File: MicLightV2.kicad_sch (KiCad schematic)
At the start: 73 parts, among them J1 12402012E212A, Q1 CSD87503Q3E, SW1 TL3365AF180QG, U1 UA78M33CKVURG3, U12 TC7PZ17FU, U2 AP33772DKZ-13, U3 STM32F072CBU6, Y1 16MHz

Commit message: REV1
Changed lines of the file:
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@@
 (kicad_sch
-	(version 20231120)
+	(version 20250114)
 	(generator "eeschema")
-	(generator_version "8.0")
+	(generator_version "9.0")
 	(paper "User" 286 260)
 	(title_block
@@
 		(company "Daxxn Industries")
 	)
+	(text "MCU GPIO"
+		(exclude_from_sim no)
+		(at 13.97 134.112 0)
+		(effects
+			(font
+				(size 2.5 2.5)
+				(thickness 0.254)
+				(bold yes)
+			)
+			(justify left)
+		)
+	)
+	(text "BUTTON FILTERING"
+		(exclude_from_sim no)
+		(at 157.226 176.276 0)
+		(effects
+			(font
+				(size 2.5 2.5)
+				(thickness 0.254)
+				(bold yes)
+			)
+			(justify left)
+		)
+	)
+	(text "INDICATORS"
+		(exclude_from_sim no)
+		(at 13.716 201.422 0)
+		(effects
+			(font
+				(size 2.5 2.5)
+				(thickness 0.254)
+				(bold yes)
+			)
+			(justify left)
+		)
+	)
+	(text "AUX POWER"
+		(exclude_from_sim no)
+		(at 186.436 16.256 0)
+		(effects
+			(font
+				(size 2.5 2.5)
+				(thickness 0.254)
+				(bold yes)
+			)
+			(justify left)
+		)
+	)
+	(text "LED DRIVERS"
+		(exclude_from_sim no)
+		(at 229.616 54.102 0)
+		(effects
+			(font
+				(size 2.5 2.5)
+				(thickness 0.254)
+				(bold yes)
+			)
+			(justify left)
+		)
+	)
+	(text "POTENTIOMETER"
+		(exclude_from_sim no)
+		(at 186.436 54.102 0)
+		(effects
+			(font
+				(size 2.5 2.5)
+				(thickness 0.254)
+				(bold yes)
+			)
+			(justify left)
+		)
+	)
+	(text "MCU POWER"
+		(exclude_from_sim no)
+		(at 157.226 97.282 0)
+		(effects
+			(font
+				(size 2.5 2.5)
+				(thickness 0.254)
+				(bold yes)
+			)
+			(justify left)
+		)
+	)
+	(text "USB POWER DELIVERY"
+		(exclude_from_sim no)
+		(at 16.51 15.24 0)
+		(effects
+			(font
+				(size 2.5 2.5)
+				(thickness 0.254)
+				(bold yes)
+			)
+			(justify left)
+		)
+	)
+	(text "MCU PROGRAMMING"
+		(exclude_from_sim no)
+		(at 13.716 97.282 0)
+		(effects
+			(font
+				(size 2.5 2.5)
+				(thickness 0.254)
+				(bold yes)
+			)
+			(justify left)
+		)
+	)
+	(text "MOUNT"
+		(exclude_from_sim no)
+		(at 128.016 201.422 0)
+		(effects
+			(font
+				(size 2.5 2.5)
+				(thickness 0.254)
+				(bold yes)
+			)
+			(justify left)
+		)
+	)
+	(text "BUTTONS"
+		(exclude_from_sim no)
+		(at 157.226 140.462 0)
+		(effects
+			(font
+				(size 2.5 2.5)
+				(thickness 0.254)
+				(bold yes)
+			)
+			(justify left)
+		)
+	)
 	(junction
 		(at 81.28 233.68)
@@
 		)
 	)
-	(text "MCU GPIO"
-		(exclude_from_sim no)
-		(at 13.97 134.112 0)
-		(effects
-			(font
-				(size 2.5 2.5)
-				(thickness 0.254)
-				(bold yes)
-			)
-			(justify left)
-		)
-	)
-	(text "BUTTON FILTERING"
-		(exclude_from_sim no)
-		(at 157.226 176.276 0)
-		(effects
-			(font
-				(size 2.5 2.5)
-				(thickness 0.254)
-				(bold yes)
-			)
-			(justify left)
-		)
-	)
-	(text "INDICATORS"
-		(exclude_from_sim no)
-		(at 13.716 201.422 0)
-		(effects
-			(font
-				(size 2.5 2.5)
-				(thickness 0.254)
-				(bold yes)
-			)
-			(justify left)
-		)
-	)
-	(text "AUX POWER"
-		(exclude_from_sim no)
-		(at 186.436 16.256 0)
-		(effects
-			(font
-				(size 2.5 2.5)
-				(thickness 0.254)
-				(bold yes)
-			)
-			(justify left)
-		)
-	)
-	(text "LED DRIVERS"
-		(exclude_from_sim no)
-		(at 229.616 54.102 0)
-		(effects
-			(font
-				(size 2.5 2.5)
-				(thickness 0.254)
-				(bold yes)
-			)
-			(justify left)
-		)
-	)
-	(text "POTENTIOMETER"
-		(exclude_from_sim no)
-		(at 186.436 54.102 0)
-		(effects
-			(font
-				(size 2.5 2.5)
-				(thickness 0.254)
-				(bold yes)
-			)
-			(justify left)
-		)
-	)
-	(text "MCU POWER"
-		(exclude_from_sim no)
-		(at 157.226 97.282 0)
-		(effects
-			(font
-				(size 2.5 2.5)
-				(thickness 0.254)
-				(bold yes)
-			)
-			(justify left)
-		)
-	)
-	(text "USB POWER DELIVERY"
-		(exclude_from_sim no)
-		(at 16.51 15.24 0)
-		(effects
-			(font
-				(size 2.5 2.5)
-				(thickness 0.254)
-				(bold yes)
-			)
-			(justify left)
-		)
-	)
-	(text "MCU PROGRAMMING"
-		(exclude_from_sim no)
-		(at 13.716 97.282 0)
-		(effects
-			(font
-				(size 2.5 2.5)
-				(thickness 0.254)
-				(bold yes)
-			)
-			(justify left)
-		)
-	)
-	(text "MOUNT"
-		(exclude_from_sim no)
-		(at 128.016 201.422 0)
-		(effects
-			(font
-				(size 2.5 2.5)
-				(thickness 0.254)
-				(bold yes)
-			)
-			(justify left)
-		)
-	)
-	(text "BUTTONS"
-		(exclude_from_sim no)
-		(at 157.226 140.462 0)
-		(effects
-			(font
-				(size 2.5 2.5)
-				(thickness 0.254)
-				(bold yes)
-			)
-			(justify left)
-		)
-	)
 	(label "LED5"
 		(at 123.19 146.05 180)
@@
 		(at 245.11 59.69)
 		(size 25.4 22.86)
+		(exclude_from_sim no)
+		(in_bom yes)
+		(on_board yes)
+		(dnp no)
 		(fields_autoplaced yes)
 		(stroke
@@
 		)
 	)
+	(embedded_fonts no)
 )

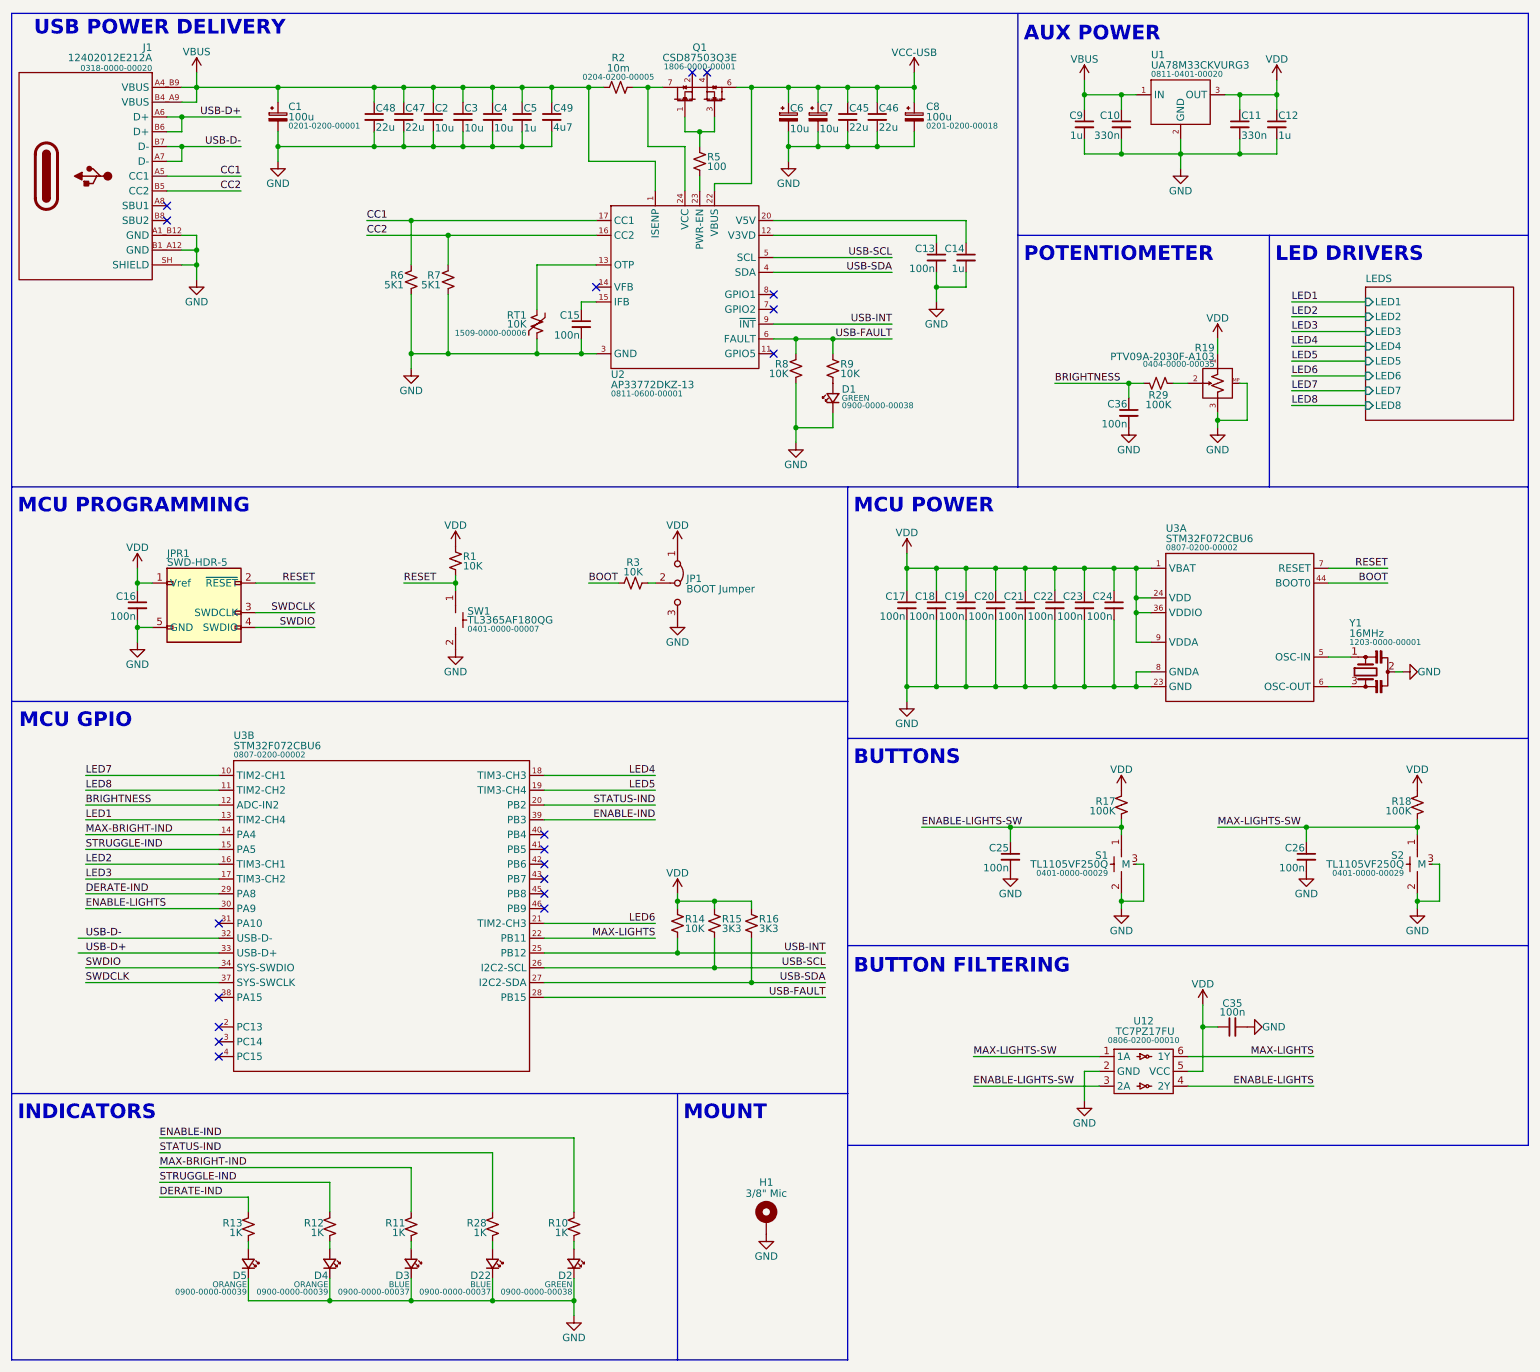
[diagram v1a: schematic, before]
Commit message: REV2 - add DAC and cc led drivers
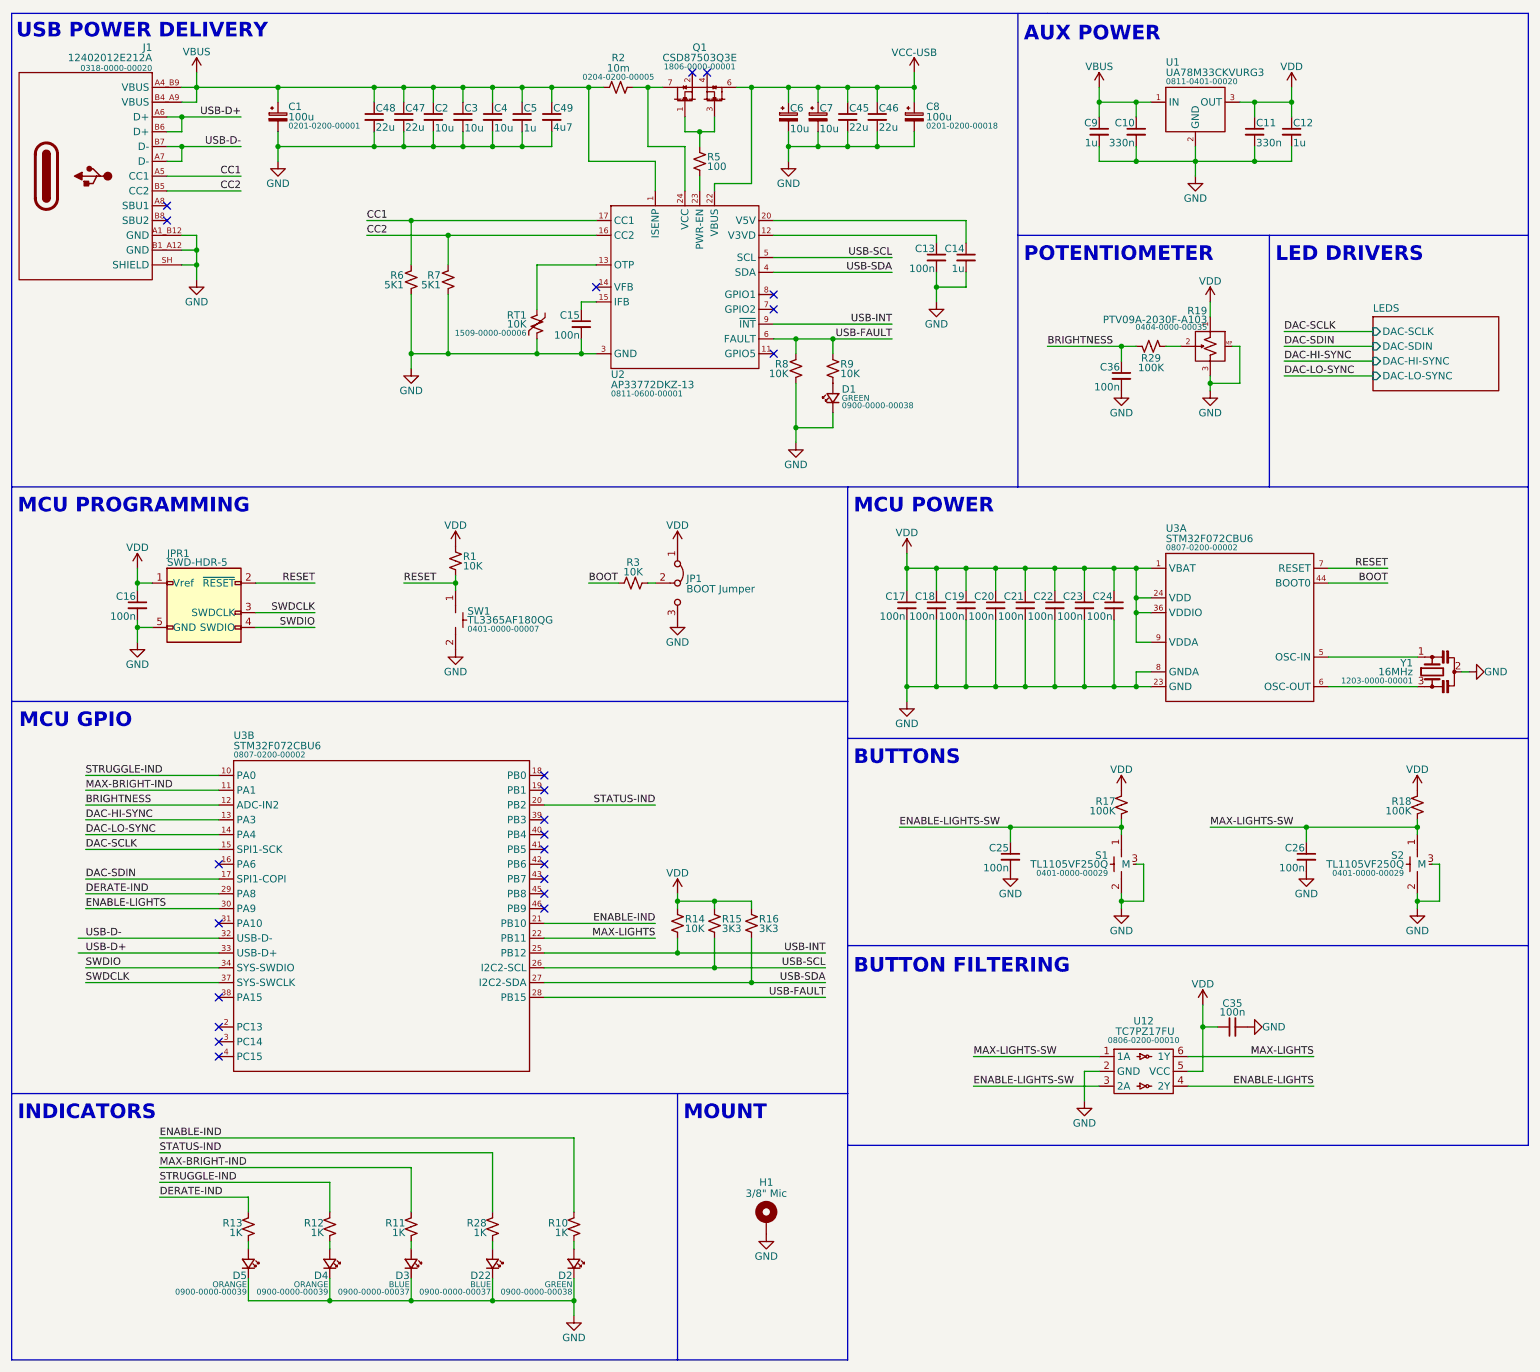
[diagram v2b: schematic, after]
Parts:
- R19: footprint Daxxn_Switches:PTV09A-2030F-A103 -> Daxxn_Controls_Pots:PTV09A-2030F-A103; symbol DX_Control_POT:PTV09A-2030F-A103 -> DX_Control_Potentiometer:PTV09A-2030F-A103
- S1, S2: footprint Daxxn_Switches:TL1105VF -> Daxxn_Controls_Buttons:TL1105VF
- SW1: footprint Daxxn_Switches:TL3365AF180QG -> Daxxn_Controls_Buttons:TL3365AF180QG
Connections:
- net LED6 is gone; now on net ENABLE-IND: U3.21 (PB10)
- net LED7 is gone; now on net STRUGGLE-IND: U3.10 (PA0)
- net LED8 is gone; now on net MAX-BRIGHT-IND: U3.11 (PA1)
- net ENABLE-IND: no longer U3.39 (PB3)
- net MAX-BRIGHT-IND: no longer U3.14 (PA4)
- net STRUGGLE-IND: no longer U3.15 (PA5)
- net LED1 renamed DAC-HI-SYNC
- net LED2: no longer names the net of U3.16 (PA6)
- net LED3 renamed DAC-SDIN
- net LED4: no longer names the net of U3.18 (PB0)
- net LED5: no longer names the net of U3.19 (PB1)
- new net DAC-LO-SYNC: U3.14 (PA4)
- new net DAC-SCLK: U3.15 (PA5)
- no-connect marks 19 -> 23
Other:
- sheet LEDS ports: added DAC-HI-SYNC, DAC-LO-SYNC, DAC-SCLK, DAC-SDIN; removed LED1, LED2, LED3, LED4, LED5, LED6, LED7, LED8
- moved on the sheet: C10, C11, C12, C36, C9, R19, R29, U1, Y1
